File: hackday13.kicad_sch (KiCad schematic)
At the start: 18 parts, among them J1 TT-output, J2 TT-input, J3 TT-bidirectional, SW1 Reset button, SW2 SW_DIP_x02, U1 RaspberryPi_Pico

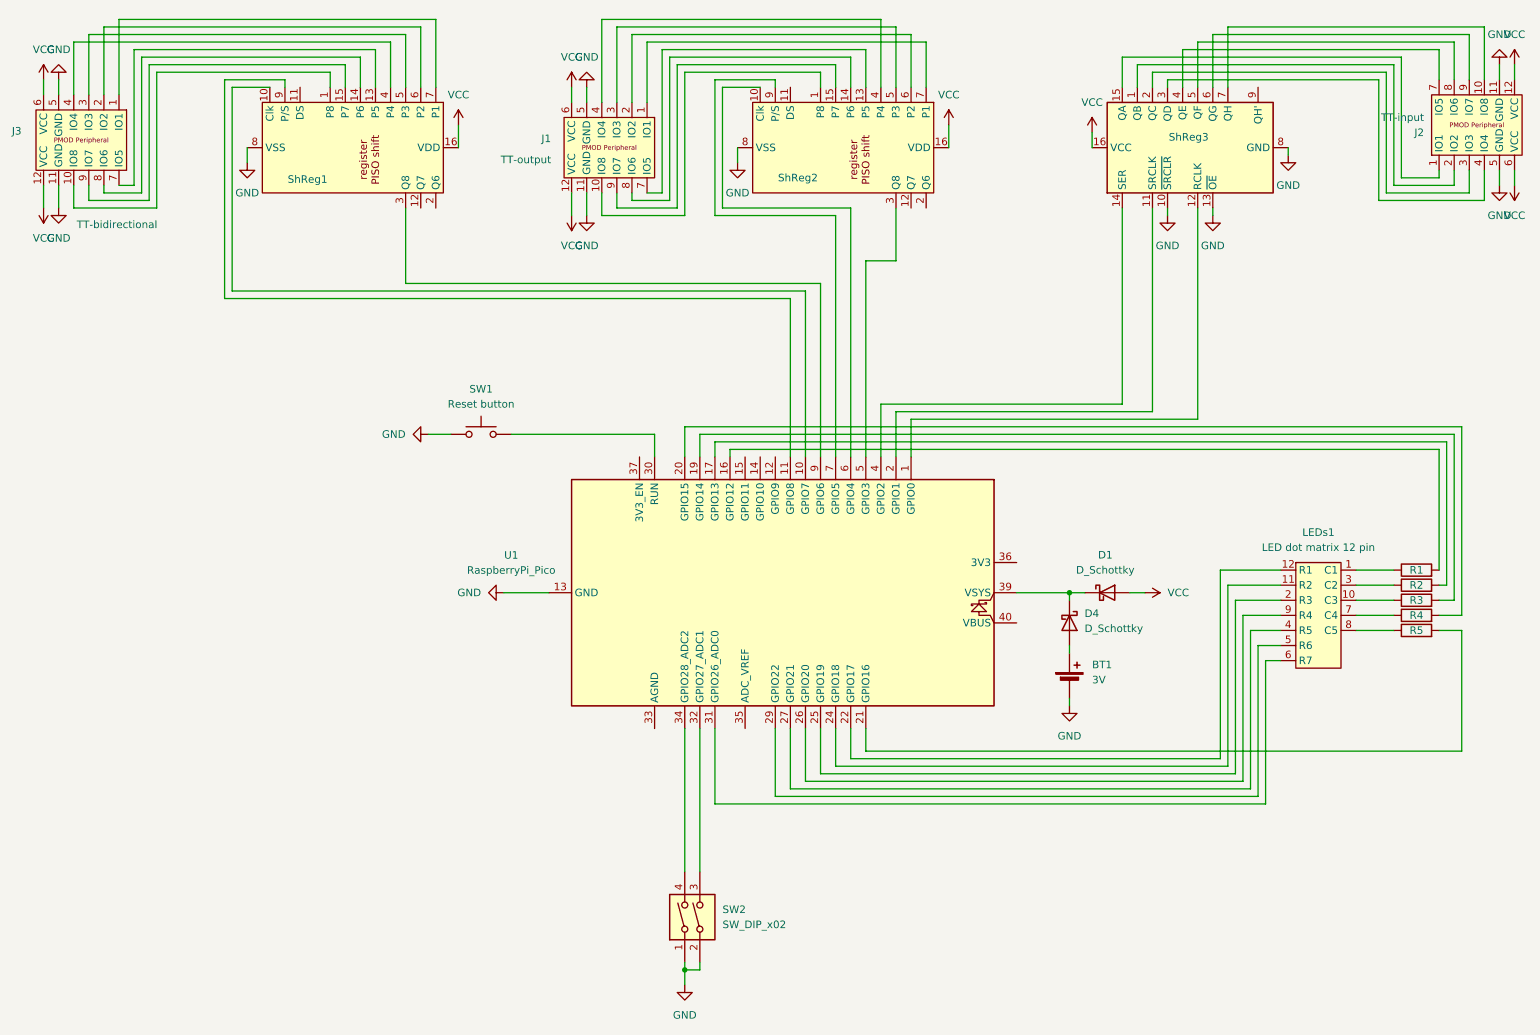
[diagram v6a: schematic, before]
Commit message: Label disconnects and power to resolve ERC checks
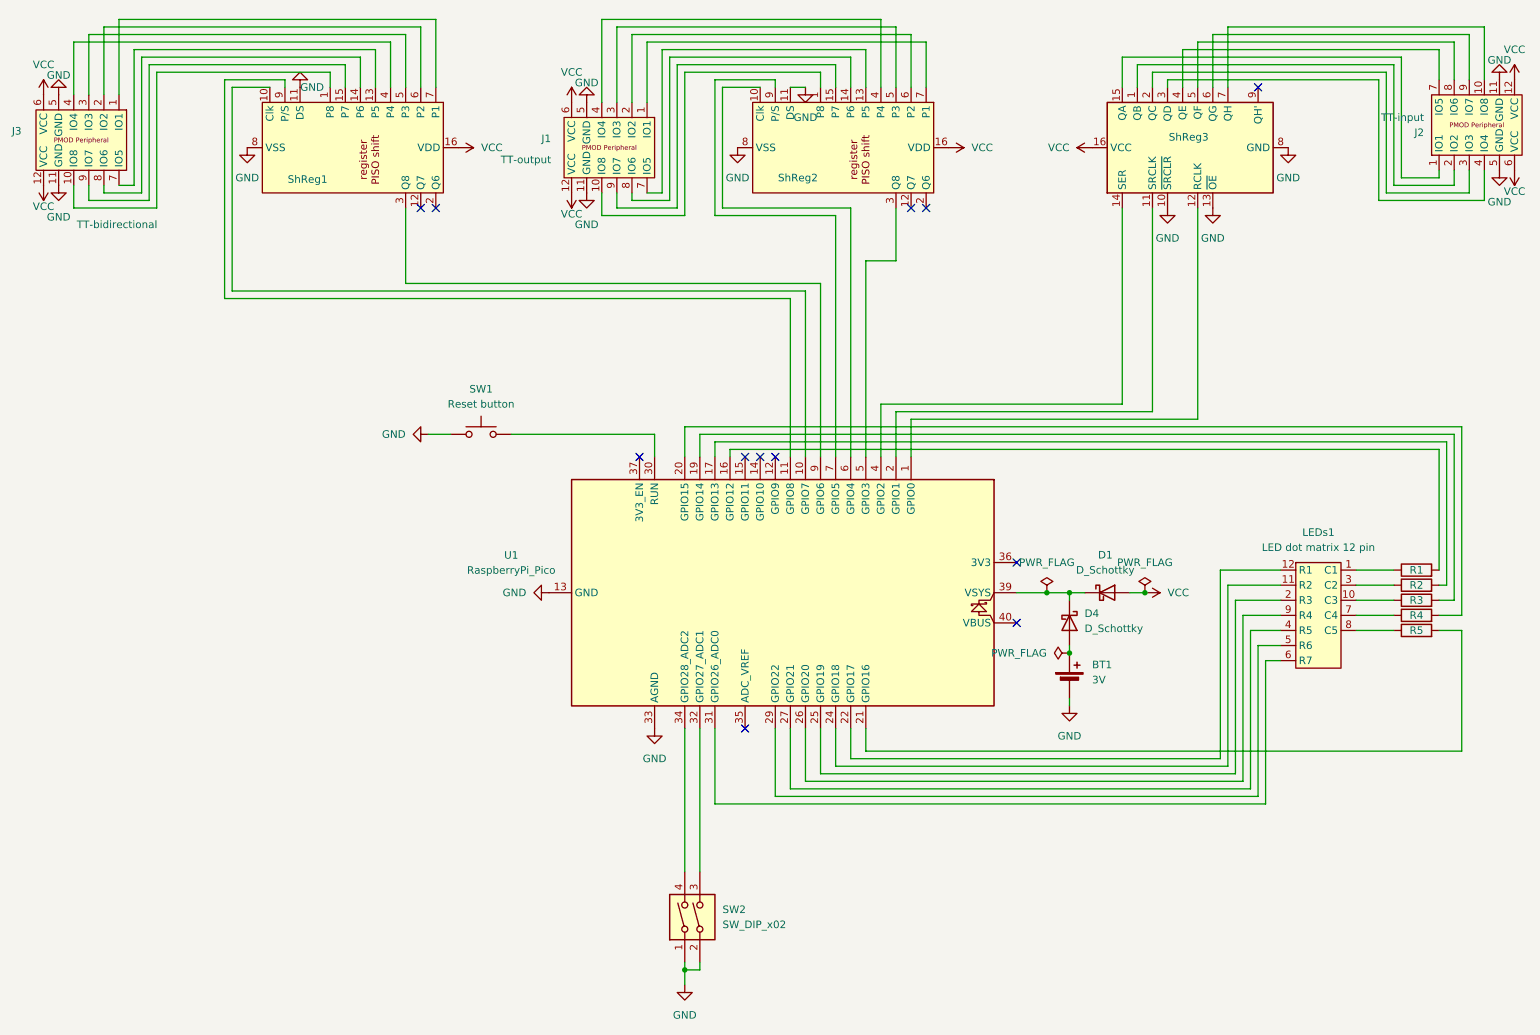
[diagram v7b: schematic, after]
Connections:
- net GND: now also ShReg1.11 (DS), ShReg2.11 (DS), U1.33 (AGND)
- no-connect marks 0 -> 12
